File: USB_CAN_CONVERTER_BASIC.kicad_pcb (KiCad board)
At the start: 2 copper layers, 30 x 19.3 mm, 23 parts, among them P1 CONN_01X04, P2 CONN_01X02, P3 USB_A, P4 CONN_01X04, U1 STM32F042C6Ux, U2 PSD2CAN, U3 SN65HVD232D, U4 MCP1700T-3302E/TT, U5 USBLC6-2

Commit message: USB and CAN connector fix
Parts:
- P3: footprint usb_ccb_custom:USB_A_DS1097 -> usb_ccb_custom:USB_A_DS1097R; moved to B.Cu
- moved P3 7.12 mm to (162.8, 94.7), turned to 270 degrees

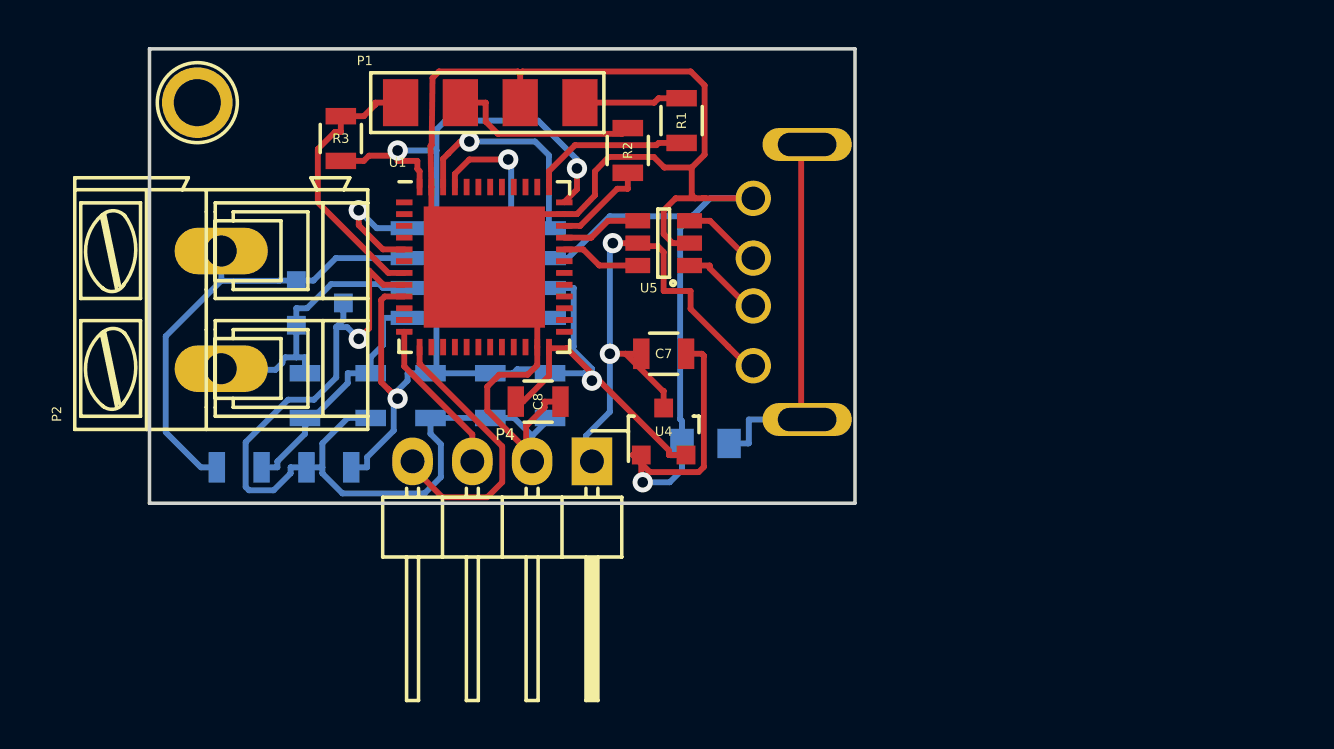
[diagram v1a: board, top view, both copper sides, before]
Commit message: UART1 switch, logo creation, CAN footprint update, botom layer replacement.
UART1 switch, logo creation, CAN footprint update, botom layer
replacement.
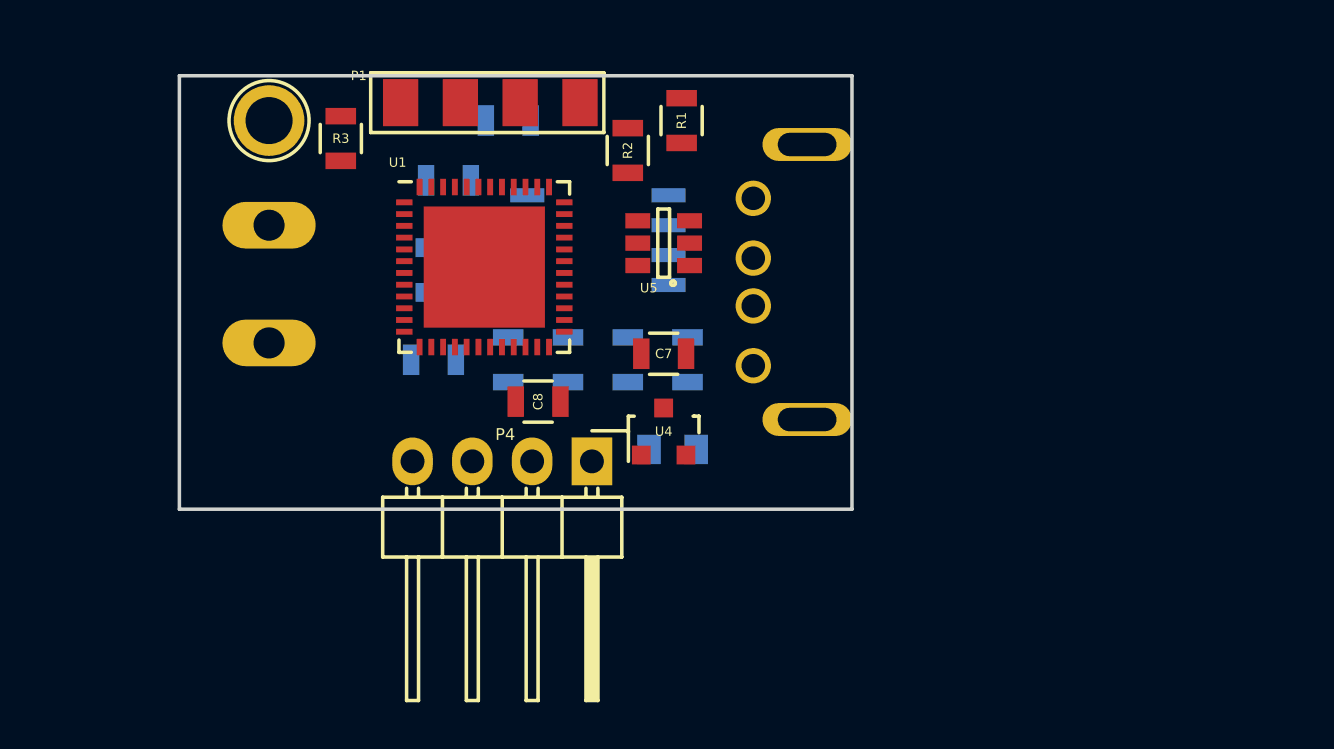
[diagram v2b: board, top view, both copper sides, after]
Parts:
- P2: moved to B.Cu
- moved C2 15.9 mm to (160.0, 101.6), turned to 270 degrees
- moved R4 15.1 mm to (149.9, 94.0)
- moved C1 13.1 mm to (152.4, 91.4), turned to 180 degrees
- moved P2 6.43 mm to (142.2, 95.9), turned to 270 degrees
- moved R5 5.67 mm to (149.2, 101.6), turned to 180 degrees
- moved U2 5.64 mm to (149.9, 97.8)
- moved U3 5.27 mm to (156.2, 96.5)
- moved C3 3.64 mm to (152.4, 101.6)
- moved C4 3.64 mm to (157.5, 101.6)
- moved C5 3.64 mm to (154.9, 101.6)
- moved REF** 3.14 mm to (142.2, 91.4)
- moved L1 1.42 mm to (159.4, 105.4)
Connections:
- P4 pad 3: /USART2_TX -> /USART1_TX
- P4 pad 4: /USART2_RX -> /USART1_RX
- R4 pad 1: Net-(P2-Pad1) -> Net-(P2-Pad2)
- R5 pad 2: Net-(P2-Pad2) -> Net-(P2-Pad1)
- U1 pad 1: Net-(U1-Pad1) -> (no net)
- U1 pad 10: Net-(U1-Pad10) -> (no net)
- U1 pad 11: Net-(U1-Pad11) -> (no net)
- U1 pad 12: /USART2_TX -> (no net)
- U1 pad 13: /USART2_RX -> (no net)
- U1 pad 14: Net-(U1-Pad14) -> (no net)
- U1 pad 15: Net-(U1-Pad15) -> (no net)
- U1 pad 16: Net-(U1-Pad16) -> (no net)
- U1 pad 17: Net-(U1-Pad17) -> (no net)
- U1 pad 18: Net-(U1-Pad18) -> (no net)
- U1 pad 19: Net-(U1-Pad19) -> (no net)
- U1 pad 2: Net-(U1-Pad2) -> (no net)
- U1 pad 20: Net-(U1-Pad20) -> (no net)
- U1 pad 21: Net-(U1-Pad21) -> (no net)
- U1 pad 22: Net-(U1-Pad22) -> (no net)
- U1 pad 25: Net-(U1-Pad25) -> (no net)
- U1 pad 26: Net-(U1-Pad26) -> (no net)
- U1 pad 27: Net-(U1-Pad27) -> (no net)
- U1 pad 28: Net-(U1-Pad28) -> (no net)
- U1 pad 29: Net-(U1-Pad29) -> (no net)
- U1 pad 3: Net-(U1-Pad3) -> (no net)
- U1 pad 30: Net-(U1-Pad30) -> /USART1_TX
- U1 pad 31: Net-(U1-Pad31) -> /USART1_RX
- U1 pad 38: Net-(U1-Pad38) -> (no net)
- U1 pad 39: Net-(U1-Pad39) -> (no net)
- U1 pad 4: Net-(U1-Pad4) -> (no net)
- U1 pad 40: Net-(U1-Pad40) -> (no net)
- U1 pad 41: Net-(U1-Pad41) -> (no net)
- U1 pad 42: Net-(U1-Pad42) -> (no net)
- U1 pad 43: Net-(U1-Pad43) -> (no net)
- U1 pad 44: Net-(U1-Pad44) -> (no net)
- U1 pad 49: GND -> (no net)
- U1 pad 6: Net-(U1-Pad6) -> (no net)
- U2 pad 1: Net-(P2-Pad2) -> Net-(P2-Pad1)
- U2 pad 2: Net-(P2-Pad1) -> Net-(P2-Pad2)
- U3 pad 6: Net-(P2-Pad2) -> Net-(P2-Pad1)
- U3 pad 7: Net-(P2-Pad1) -> Net-(P2-Pad2)
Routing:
- net GND: track 131.6 -> 0.00 mm, vias 2 -> 0
- net +3V3: track 62.7 -> 0.00 mm, vias 4 -> 0
- net +5V: track 24.1 -> 0.00 mm, vias 2 -> 0
- net Net-(P2-Pad1): track 19.8 -> 0.00 mm
- net Net-(L1-Pad2): track 15.8 -> 0.00 mm
- net /USART2_RX: track 12.3 -> 0.00 mm
- net Net-(P2-Pad2): track 12.2 -> 0.00 mm
- net Net-(P1-Pad1): track 12.0 -> 0.00 mm
- net CAN_RX: track 11.3 -> 0.00 mm, vias 1 -> 0
- net Net-(C1-Pad2): track 10.8 -> 0.00 mm
- net CAN_TX: track 9.34 -> 0.00 mm, vias 1 -> 0
- net Net-(P1-Pad2): track 8.23 -> 0.00 mm
- net SW_CLK: track 6.80 -> 0.00 mm
- net /USART2_TX: track 6.70 -> 0.00 mm
- net CAN_MOD: track 5.39 -> 0.00 mm, vias 1 -> 0
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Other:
- board size 30 x 19.3 mm -> 28.6 x 18.4 mm
- board text added: "+5V"
- board text added: "CAN"
- board text added: "DEVICES"
- board text added: "GND"
- board text added: "RX"
- board text added: "TX"
- board text added: "U"
- board text added: "UUCC1.0"

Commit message: SWD connector update, logo generation,  board otline update.
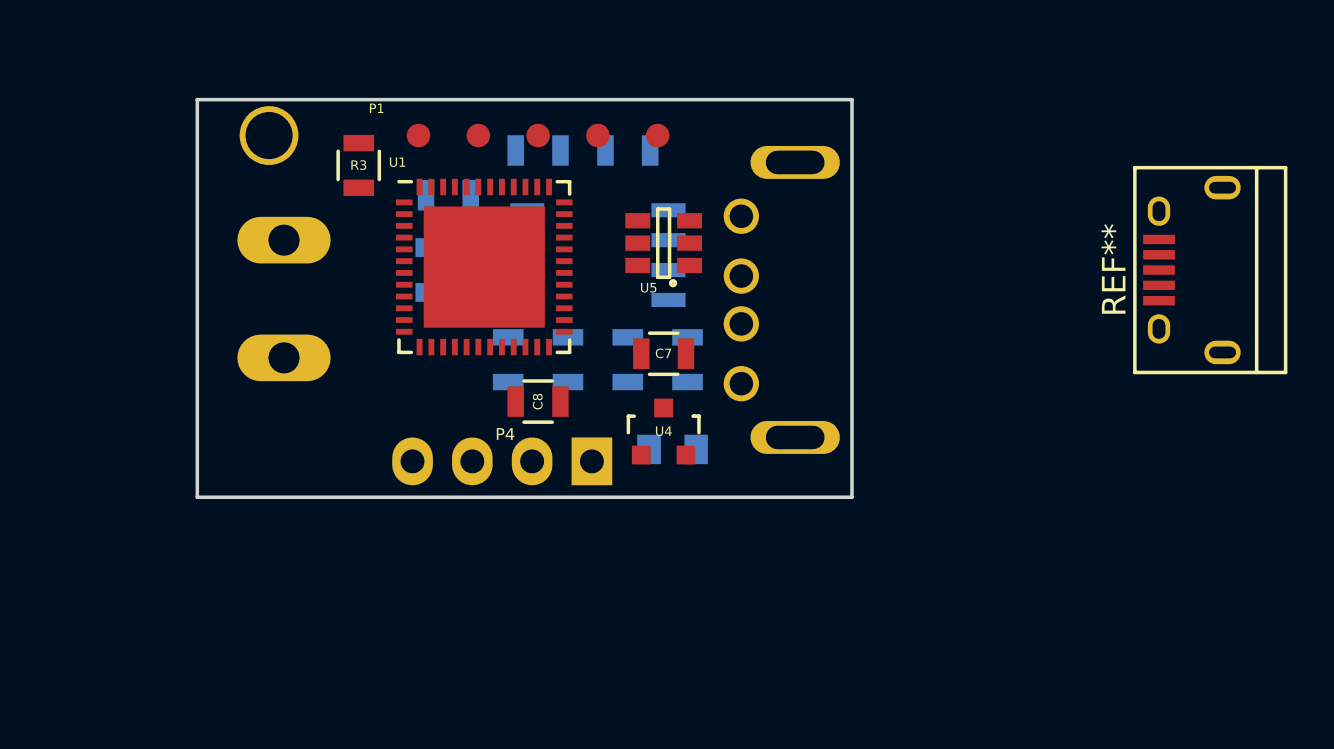
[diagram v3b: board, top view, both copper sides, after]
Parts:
- removed R1, R2: 20, Resistors_SMD:R_0805
- added REF**: USB_Micro-B, Connect:USB_Micro-B, F.Cu at (181.6, 97.8)
- P1: value CONN_01X04 -> CONN_01X05; footprint usb_ccb_custom:swd_smd_conn -> usb_ccb_custom:swd_smd_conn5
- P4: footprint Pin_Headers:Pin_Header_Angled_1x04 -> usb_ccb_custom:Pin_Header_Angled_1x04m
- moved R5 7.01 mm to (149.9, 94.6)
- moved C1 5.24 mm to (157.5, 92.7)
- moved R4 4.02 mm to (153.7, 92.7)
- moved P1 1.59 mm to (152.4, 92.1)
- moved R3 1.37 mm to (146.1, 93.3)
- moved P3 0.92 mm to (162.3, 95.5)
- moved P2 0.90 mm to (142.9, 96.5)
- moved REF** 0.64 mm to (142.2, 92.1)
- moved U3 0.64 mm to (156.2, 97.2)
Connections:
- P1 pad 1: Net-(P1-Pad1) -> +3V3
- P1 pad 3: GND -> SW_CLK
- P1 pad 4: Net-(P1-Pad4) -> GND
- R3 pad 1: Net-(P1-Pad1) -> Net-(P1-Pad2)
- U1 pad 7: Net-(P1-Pad1) -> Net-(P1-Pad2)
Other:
- board size 28.6 x 18.4 mm -> 27.8 x 16.9 mm

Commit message: CAN Jumpers addition
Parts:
- added GS1: GS2, Connect:GS2, F.Cu at (147.8, 110.9)
- added GS2: GS2, Connect:GS2, F.Cu at (151.6, 111.2)
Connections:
- P2 pad 1: Net-(P2-Pad1) -> Net-(GS2-Pad2)
- P2 pad 2: Net-(P2-Pad2) -> Net-(GS1-Pad2)
- R4 pad 1: Net-(P2-Pad2) -> Net-(GS1-Pad1)
- R5 pad 2: Net-(P2-Pad1) -> Net-(GS2-Pad1)
- U2 pad 1: Net-(P2-Pad1) -> Net-(GS2-Pad2)
- U2 pad 2: Net-(P2-Pad2) -> Net-(GS1-Pad2)
- U3 pad 6: Net-(P2-Pad1) -> Net-(GS2-Pad2)
- U3 pad 7: Net-(P2-Pad2) -> Net-(GS1-Pad2)

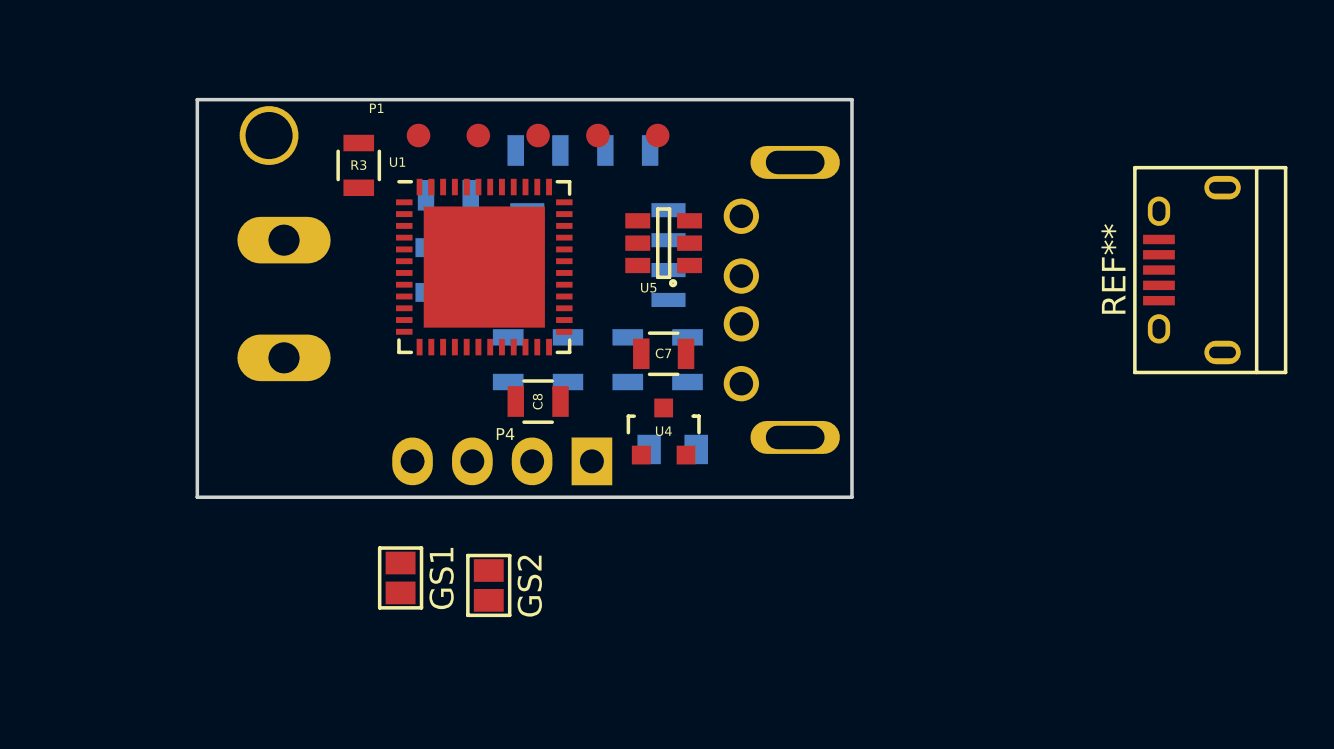
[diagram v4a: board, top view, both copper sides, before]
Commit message: Outline size reduction
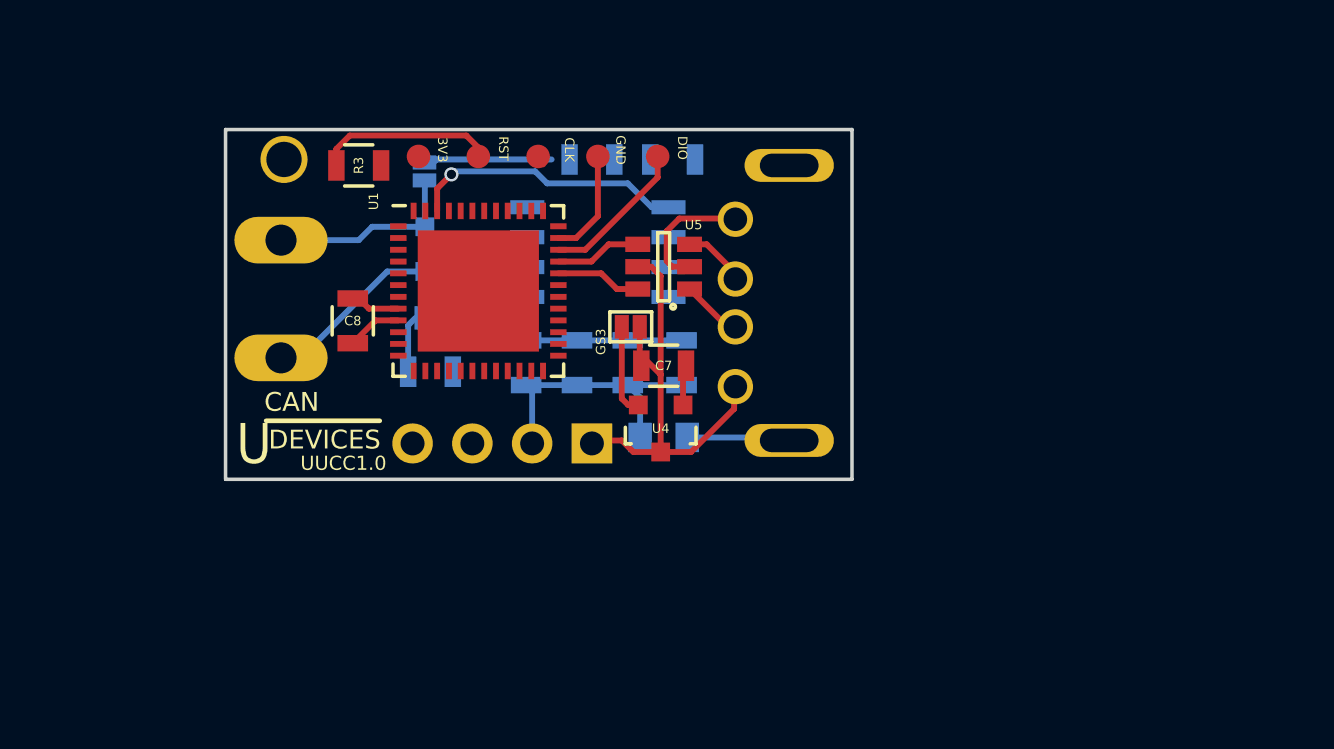
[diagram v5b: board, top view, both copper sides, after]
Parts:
- removed the REF** at (181.6, 97.8)
- added GS3: GS2, usb_ccb_custom:GS2s, F.Cu at (157.6, 100.2)
- C4: value C -> 10nC
- C5: value C -> 100nC
- GS1, GS2: footprint Connect:GS2 -> usb_ccb_custom:GS2s; moved to B.Cu
- moved GS1 17.3 mm to (148.8, 93.6), turned to 180 degrees
- moved GS2 11.6 mm to (149.1, 99.8), turned to 270 degrees
- moved C8 8.59 mm to (145.8, 99.9), turned to 90 degrees
- moved R5 7.53 mm to (149.1, 102.1)
- moved R4 2.32 mm to (156.0, 93.1)
- moved C1 1.94 mm to (159.4, 93.1)
- moved REF** 1.20 mm to (142.9, 93.1)
- moved U1 1.05 mm to (151.1, 98.7)
- moved U5 1.00 mm to (159.0, 97.6)
- moved U2 0.89 mm to (149.9, 96.9)
- moved P1 0.89 mm to (152.4, 93.0)
- moved C3 0.77 mm to (153.2, 101.7)
- moved P4 0.76 mm to (156.0, 105.2)
- moved L1 0.63 mm to (159.0, 104.9)
- moved C7 0.51 mm to (159.0, 101.9)
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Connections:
- U1 pad 1: (no net) -> Net-(U1-Pad1)
- U1 pad 10: (no net) -> Net-(U1-Pad10)
- U1 pad 11: (no net) -> Net-(U1-Pad11)
- U1 pad 12: (no net) -> Net-(U1-Pad12)
- U1 pad 13: (no net) -> Net-(U1-Pad13)
- U1 pad 14: (no net) -> Net-(U1-Pad14)
- U1 pad 15: (no net) -> Net-(U1-Pad15)
- U1 pad 16: (no net) -> Net-(U1-Pad16)
- U1 pad 17: (no net) -> Net-(U1-Pad17)
- U1 pad 18: (no net) -> Net-(U1-Pad18)
- U1 pad 19: (no net) -> Net-(U1-Pad19)
- U1 pad 2: (no net) -> Net-(U1-Pad2)
- U1 pad 20: (no net) -> Net-(U1-Pad20)
- U1 pad 21: (no net) -> Net-(U1-Pad21)
- U1 pad 22: (no net) -> Net-(U1-Pad22)
- U1 pad 25: (no net) -> Net-(U1-Pad25)
- U1 pad 26: (no net) -> Net-(U1-Pad26)
- U1 pad 27: (no net) -> Net-(U1-Pad27)
- U1 pad 28: (no net) -> Net-(U1-Pad28)
- U1 pad 29: (no net) -> Net-(U1-Pad29)
- U1 pad 3: (no net) -> Net-(U1-Pad3)
- U1 pad 38: (no net) -> Net-(U1-Pad38)
- U1 pad 39: (no net) -> Net-(U1-Pad39)
- U1 pad 4: (no net) -> Net-(U1-Pad4)
- U1 pad 40: (no net) -> Net-(U1-Pad40)
- U1 pad 41: (no net) -> Net-(U1-Pad41)
- U1 pad 42: (no net) -> Net-(U1-Pad42)
- U1 pad 43: (no net) -> Net-(U1-Pad43)
- U1 pad 44: (no net) -> Net-(U1-Pad44)
- U1 pad 6: (no net) -> Net-(U1-Pad6)
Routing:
- net GND: track 0.00 -> 25.7 mm
- net +5V: track 0.00 -> 19.5 mm
- net +3V3: track 0.00 -> 12.6 mm
- net CAN_TX: track 0.00 -> 11.7 mm, vias 0 -> 1
- net Net-(GS2-Pad2): track 0.00 -> 10.0 mm
- net Net-(GS1-Pad2): track 0.00 -> 8.18 mm
- net Net-(P1-Pad2): track 0.00 -> 7.69 mm
- net SW_DIO: track 0.00 -> 6.26 mm
- net Net-(GS1-Pad1): track 0.00 -> 5.45 mm
- net Net-(L1-Pad2): track 0.00 -> 4.32 mm
- net Net-(U1-Pad33): track 0.00 -> 3.68 mm
- net Net-(U1-Pad32): track 0.00 -> 3.65 mm
- net Net-(P3-Pad3): track 0.00 -> 2.65 mm
- net Net-(P3-Pad2): track 0.00 -> 2.55 mm
- net Net-(GS2-Pad1): track 0.00 -> 2.42 mm
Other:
- board size 27.8 x 16.9 mm -> 26.6 x 14.9 mm
- board text added: "3V3"
- board text added: "CLK"
- board text added: "DIO"
- board text added: "RST"
